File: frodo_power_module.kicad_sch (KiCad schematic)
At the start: 78 parts, among them J1 Keystone 1098, J10 SWD Header, J2 Molex MicroFit 2x2, J3 Molex MicroFit 2x2, J4 Molex MicroFit 2x2, J5 Molex MicroFit 2x2, J6 Molex MicroFit 2x2, J7 JST-GH, J8 JST-GH, J9 JST-GH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

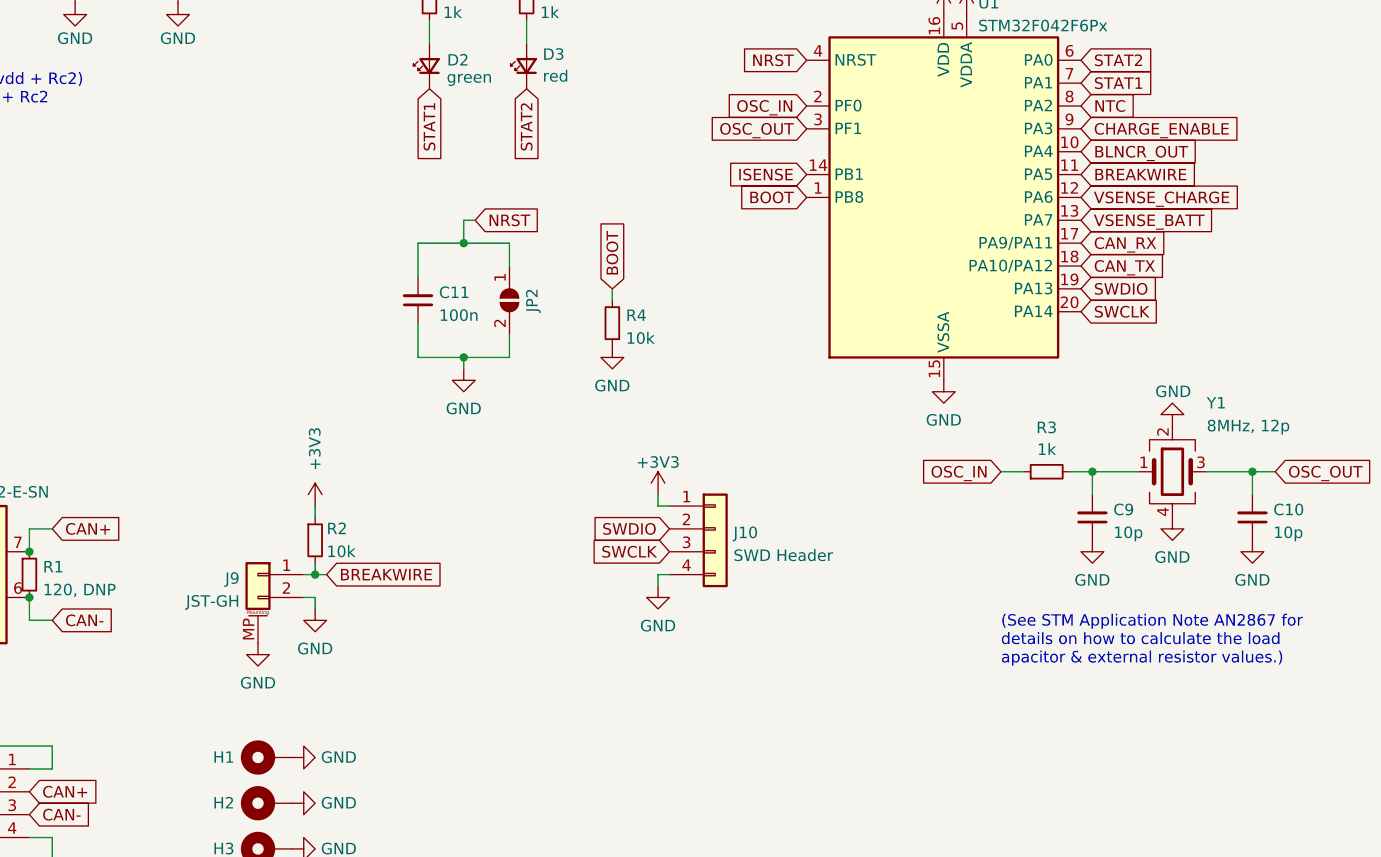
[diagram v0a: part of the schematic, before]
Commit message: removed breakwire system
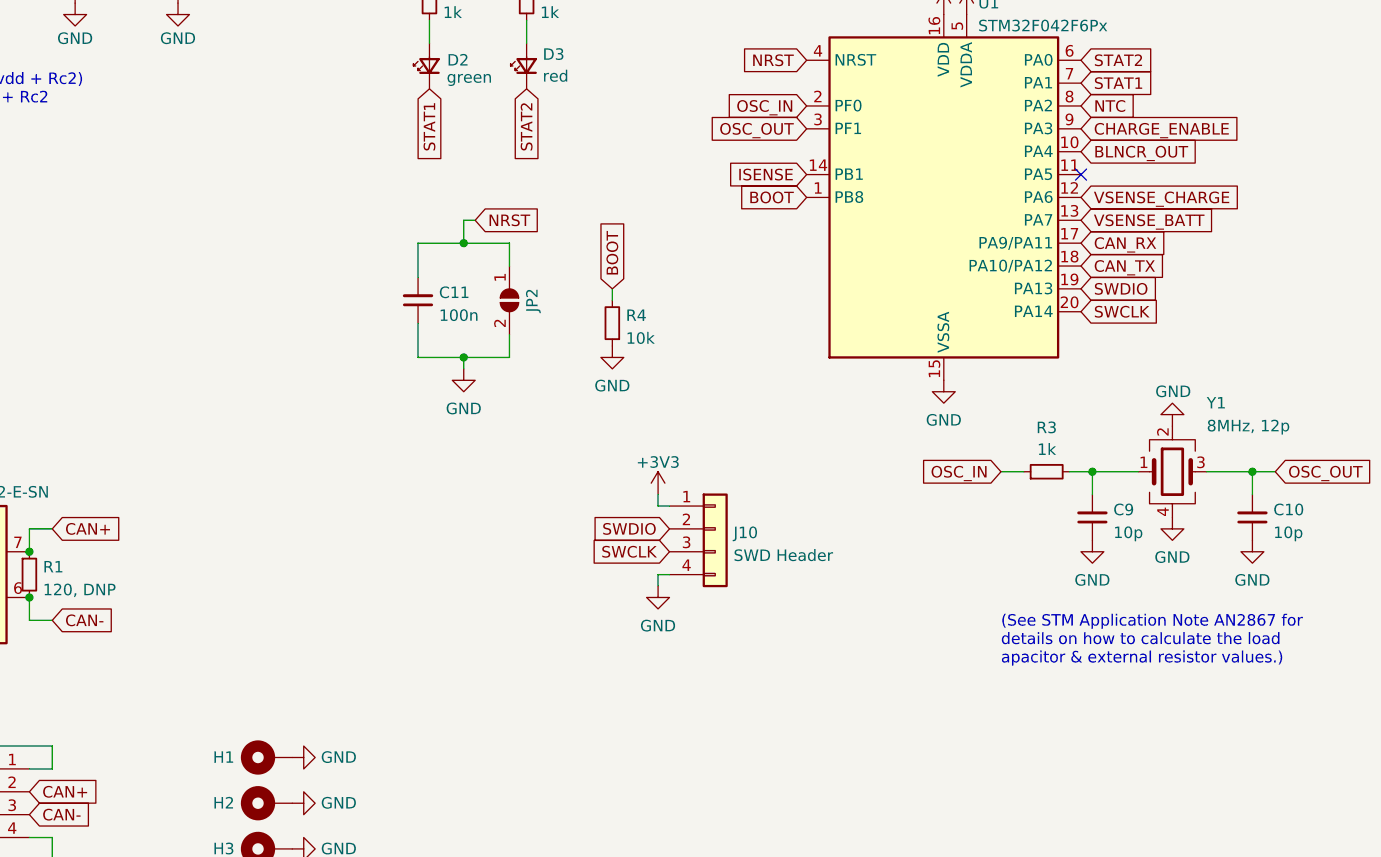
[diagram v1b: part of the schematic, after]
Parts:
- removed J9: JST-GH, Connector_JST:JST_GH_SM02B-GHS-TB_1x02-1MP_P1.25mm_Horizontal, symbol Connector_Generic_MountingPin:Conn_01x02_MountingPin
- removed R2: 10k, Resistor_SMD:R_0603_1608Metric, symbol Device:R_Small
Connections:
- net BREAKWIRE: no longer names the net of U1.11 (PA5)
- no-connect marks 0 -> 1
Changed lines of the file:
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@@
   (junction (at 44.45 161.29) (diameter 0) (color 0 0 0 0)
   )
-  (junction (at 165.1 152.4) (diameter 0) (color 0 0 0 0)
-  )
   (junction (at 205.74 31.75) (diameter 0) (color 0 0 0 0)
   )
@@
   (junction (at 44.45 154.94) (diameter 0) (color 0 0 0 0)
   )
+  (no_connect (at 250.19 107.95))
   (wire (pts (xy 135.89 181.61) (xy 135.89 184.15))
     (stroke (width 0) (type default))
@@
     (stroke (width 0) (type default))
   )
-  (wire (pts (xy 165.1 154.94) (xy 165.1 156.21))
-    (stroke (width 0) (type default))
-  )
   (wire (pts (xy 215.9 66.04) (xy 220.98 66.04))
     (stroke (width 0) (type default))
@@
     (stroke (width 0) (type default))
   )
-  (wire (pts (xy 165.1 151.13) (xy 165.1 152.4))
-    (stroke (width 0) (type default))
-  )
   (wire (pts (xy 220.98 76.2) (xy 220.98 77.47))
     (stroke (width 0) (type default))
@@
     (stroke (width 0) (type default))
   )
-  (wire (pts (xy 165.1 152.4) (xy 166.37 152.4))
-    (stroke (width 0) (type default))
-  )
   (wire (pts (xy 101.6 49.53) (xy 115.57 49.53))
     (stroke (width 0) (type default))
@@
     (stroke (width 0) (type default))
   )
-  (wire (pts (xy 163.83 152.4) (xy 165.1 152.4))
-    (stroke (width 0) (type default))
-  )
   (wire (pts (xy 44.45 176.53) (xy 44.45 177.8))
     (stroke (width 0) (type default))
@@
     (stroke (width 0) (type default))
   )
-  (wire (pts (xy 165.1 144.78) (xy 165.1 146.05))
-    (stroke (width 0) (type default))
-  )
   (wire (pts (xy 204.47 152.4) (xy 203.2 152.4))
     (stroke (width 0) (type default))
@@
     (stroke (width 0) (type default))
   )
-  (wire (pts (xy 163.83 154.94) (xy 165.1 154.94))
-    (stroke (width 0) (type default))
-  )
   (wire (pts (xy 21.59 67.31) (xy 21.59 71.12))
     (stroke (width 0) (type default))
@@
     )
   )
-  (global_label "BREAKWIRE" (shape input) (at 166.37 152.4 0) (fields_autoplaced)
-    (effects (font (size 1.27 1.27)) (justify left))
-    (property "Intersheetrefs" "${INTERSHEET_REFS}" (at 179.7986 152.4 0)
-      (effects (font (size 1.27 1.27)) (justify left) hide)
-    )
-  )
   (global_label "SWDIO" (shape input) (at 204.47 147.32 180) (fields_autoplaced)
     (effects (font (size 1.27 1.27)) (justify right))
@@
     )
   )
-  (global_label "BREAKWIRE" (shape input) (at 250.19 107.95 0) (fields_autoplaced)
-    (effects (font (size 1.27 1.27)) (justify left))
-    (property "Intersheetrefs" "${INTERSHEET_REFS}" (at 263.6186 107.95 0)
-      (effects (font (size 1.27 1.27)) (justify left) hide)
-    )
-  )
   (global_label "OSC_IN" (shape input) (at 219.71 100.33 180) (fields_autoplaced)
     (effects (font (size 1.27 1.27)) (justify right))
@@
     )
   )
-  (symbol (lib_id "Device:R_Small") (at 165.1 148.59 0) (unit 1)
-    (in_bom yes) (on_board yes) (dnp no)
-    (property "Reference" "R2" (at 166.37 147.32 0)
-      (effects (font (size 1.27 1.27)) (justify left))
-    )
-    (property "Value" "10k" (at 166.37 149.86 0)
-      (effects (font (size 1.27 1.27)) (justify left))
-    )
-    (property "Footprint" "Resistor_SMD:R_0603_1608Metric" (at 165.1 148.59 0)
-      (effects (font (size 1.27 1.27)) hide)
-    )
-    (property "Datasheet" "~" (at 165.1 148.59 0)
-      (effects (font (size 1.27 1.27)) hide)
-    )
-    (property "LCSC#" "C98220" (at 165.1 148.59 0)
-      (effects (font (size 1.27 1.27)) hide)
-    )
-    (property "Manufacturer" "YAGEO" (at 165.1 148.59 0)
-      (effects (font (size 1.27 1.27)) hide)
-    )
-    (property "Part#" "RC0603FR-0710KL" (at 165.1 148.59 0)
-      (effects (font (size 1.27 1.27)) hide)
-    )
-    (pin "1")
-    (pin "2")
-    (instances
-      (project "frodo_power_module"
-        (path "/afc8cbd3-9ea8-40a2-afae-ed6bd0fe7e6e"
-          (reference "R2") (unit 1)
-        )
-      )
-      (project "euroc_fc"
-        (path "/e63e39d7-6ac0-4ffd-8aa3-1841a4541b55"
-          (reference "R23") (unit 1)
-        )
-      )
-    )
-  )
   (symbol (lib_id "power:GND") (at 260.35 135.89 180) (unit 1)
     (in_bom yes) (on_board yes) (dnp no)
@@
     )
   )
-  (symbol (lib_id "power:+3V3") (at 165.1 144.78 0) (unit 1)
-    (in_bom yes) (on_board yes) (dnp no)
-    (property "Reference" "#PWR027" (at 165.1 148.59 0)
-      (effects (font (size 1.27 1.27)) hide)
-    )
-    (property "Value" "+3V3" (at 165.1 138.43 90)
-      (effects (font (size 1.27 1.27)))
-    )
-    (property "Footprint" "" (at 165.1 144.78 0)
-      (effects (font (size 1.27 1.27)) hide)
-    )
-    (property "Datasheet" "" (at 165.1 144.78 0)
-      (effects (font (size 1.27 1.27)) hide)
-    )
-    (pin "1")
-    (instances
-      (project "frodo_power_module"
-        (path "/afc8cbd3-9ea8-40a2-afae-ed6bd0fe7e6e"
-          (reference "#PWR027") (unit 1)
-        )
-      )
-      (project "euroc_fc"
-        (path "/e63e39d7-6ac0-4ffd-8aa3-1841a4541b55"
-          (reference "#PWR029") (unit 1)
-        )
-      )
-    )
-  )
   (symbol (lib_id "Regulator_Linear:AZ1117-3.3") (at 255.27 27.94 0) (unit 1)
     (in_bom yes) (on_board yes) (dnp no) (fields_autoplaced)
@@
     )
   )
-  (symbol (lib_id "power:GND") (at 165.1 156.21 0) (mirror y) (unit 1)
-    (in_bom yes) (on_board yes) (dnp no) (fields_autoplaced)
-    (property "Reference" "#PWR035" (at 165.1 162.56 0)
-      (effects (font (size 1.27 1.27)) hide)
-    )
-    (property "Value" "GND" (at 165.1 160.6534 0)
-      (effects (font (size 1.27 1.27)))
-    )
-    (property "Footprint" "" (at 165.1 156.21 0)
-      (effects (font (size 1.27 1.27)) hide)
-    )
-    (property "Datasheet" "" (at 165.1 156.21 0)
-      (effects (font (size 1.27 1.27)) hide)
-    )
-    (pin "1")
-    (instances
-      (project "frodo_power_module"
-        (path "/afc8cbd3-9ea8-40a2-afae-ed6bd0fe7e6e"
-          (reference "#PWR035") (unit 1)
-        )
-      )
-      (project "euroc_fc"
-        (path "/e63e39d7-6ac0-4ffd-8aa3-1841a4541b55"
-          (reference "#PWR0169") (unit 1)
-        )
-      )
-    )
-  )
   (symbol (lib_id "power:+VSW") (at 45.72 161.29 270) (mirror x) (unit 1)
     (in_bom yes) (on_board yes) (dnp no) (fields_autoplaced)
@@
     )
   )
-  (symbol (lib_id "Connector_Generic_MountingPin:Conn_01x02_MountingPin") (at 158.75 152.4 0) (mirror y) (unit 1)
-    (in_bom yes) (on_board yes) (dnp no) (fields_autoplaced)
-    (property "Reference" "J9" (at 156.718 152.8353 0)
-      (effects (font (size 1.27 1.27)) (justify left))
-    )
-    (property "Value" "JST-GH" (at 156.718 155.3722 0)
-      (effects (font (size 1.27 1.27)) (justify left))
-    )
-    (property "Footprint" "Connector_JST:JST_GH_SM02B-GHS-TB_1x02-1MP_P1.25mm_Horizontal" (at 158.75 152.4 0)
-      (effects (font (size 1.27 1.27)) hide)
-    )
-    (property "Datasheet" "~" (at 158.75 152.4 0)
-      (effects (font (size 1.27 1.27)) hide)
-    )
-    (property "LCSC#" "C189893" (at 158.75 152.4 0)
-      (effects (font (size 1.27 1.27)) hide)
-    )
-    (property "Manufacturer" "JST" (at 158.75 152.4 0)
-      (effects (font (size 1.27 1.27)) hide)
-    )
-    (property "Part#" "SM02B-GHS-TB" (at 158.75 152.4 0)
-      (effects (font (size 1.27 1.27)) hide)
-    )
-    (pin "1")
-    (pin "2")
-    (pin "MP")
-    (instances
-      (project "frodo_power_module"
-        (path "/afc8cbd3-9ea8-40a2-afae-ed6bd0fe7e6e"
-          (reference "J9") (unit 1)
-        )
-      )
-      (project "euroc_fc"
-        (path "/e63e39d7-6ac0-4ffd-8aa3-1841a4541b55"
-          (reference "J6") (unit 1)
-        )
-      )
-    )
-  )
   (symbol (lib_id "Device:C_Small") (at 176.53 121.92 180) (unit 1)
     (in_bom yes) (on_board yes) (dnp no)
@@
         )
       )
-    )
-  )
-  (symbol (lib_id "power:GND") (at 158.75 160.02 0) (mirror y) (unit 1)
-    (in_bom yes) (on_board yes) (dnp no) (fields_autoplaced)
-    (property "Reference" "#PWR020" (at 158.75 166.37 0)
-      (effects (font (size 1.27 1.27)) hide)
-    )
-    (property "Value" "GND" (at 158.75 164.4634 0)
-      (effects (font (size 1.27 1.27)))
-    )
-    (property "Footprint" "" (at 158.75 160.02 0)
-      (effects (font (size 1.27 1.27)) hide)
-    )
-    (property "Datasheet" "" (at 158.75 160.02 0)
-      (effects (font (size 1.27 1.27)) hide)
-    )
-    (pin "1")
-    (instances
-      (project "frodo_power_module"
-        (path "/afc8cbd3-9ea8-40a2-afae-ed6bd0fe7e6e"
-          (reference "#PWR020") (unit 1)
-        )
-      )
-      (project "euroc_fc"
-        (path "/e63e39d7-6ac0-4ffd-8aa3-1841a4541b55"
-          (reference "#PWR0169") (unit 1)
-        )
-      )

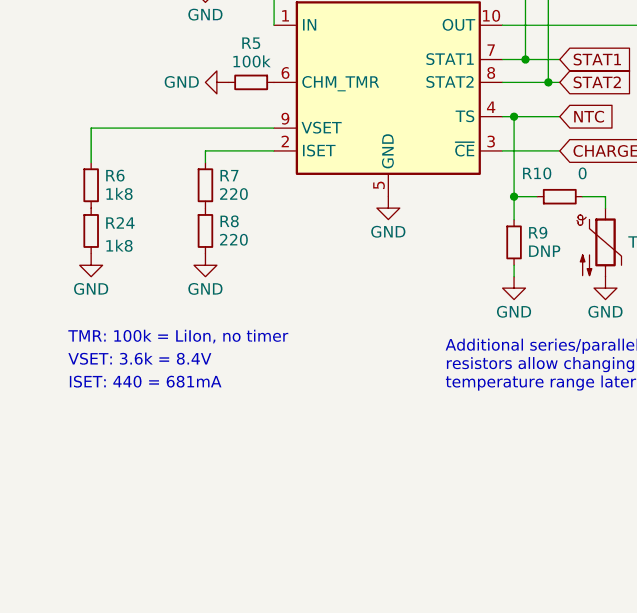
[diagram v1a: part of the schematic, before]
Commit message: removed breakwire and changed Iset resistance from 440 to 390 to achieve approx 800mA charging
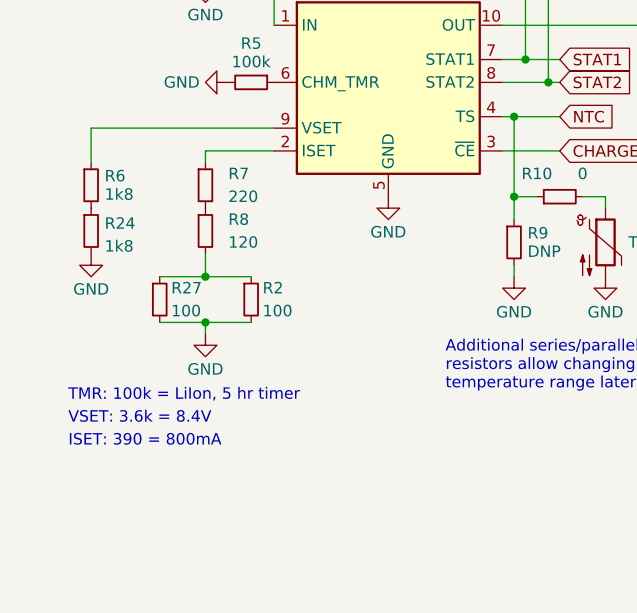
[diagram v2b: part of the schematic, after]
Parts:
- added R2, R27: 100, Resistor_SMD:R_0603_1608Metric, symbol Device:R_Small
- R8: value 220 -> 120
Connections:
- net GND: now also R2.2, R27.2; no longer R8.2
- new net: R2.1, R27.1, R8.2
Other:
- note added: "ISET: 390 = 800mA"
- note added: "TMR: 100k = LiIon, 5 hr timer"
- note removed: "ISET: 440 = 681mA"
- note removed: "TMR: 100k = LiIon, no timer"
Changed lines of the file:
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@@
   (junction (at 223.52 31.75) (diameter 0) (color 0 0 0 0)
   )
+  (junction (at 34.29 83.82) (diameter 0) (color 0 0 0 0)
+  )
   (junction (at 133.35 154.94) (diameter 0) (color 0 0 0 0)
   )
@@
   (junction (at 251.46 140.97) (diameter 0) (color 0 0 0 0)
   )
+  (junction (at 34.29 88.9) (diameter 0) (color 0 0 0 0)
+  )
   (junction (at 165.1 67.31) (diameter 0) (color 0 0 0 0)
   )
@@
     (stroke (width 0) (type default))
   )
+  (wire (pts (xy 34.29 88.9) (xy 34.29 90.17))
+    (stroke (width 0) (type default))
+  )
+  (wire (pts (xy 34.29 83.82) (xy 39.37 83.82))
+    (stroke (width 0) (type default))
+  )
   (wire (pts (xy 121.92 62.23) (xy 121.92 64.77))
     (stroke (width 0) (type default))
@@
     (stroke (width 0) (type default))
   )
+  (wire (pts (xy 29.21 88.9) (xy 34.29 88.9))
+    (stroke (width 0) (type default))
+  )
   (wire (pts (xy 76.2 74.93) (xy 78.74 74.93))
     (stroke (width 0) (type default))
@@
     (stroke (width 0) (type default))
   )
+  (wire (pts (xy 34.29 81.28) (xy 34.29 83.82))
+    (stroke (width 0) (type default))
+  )
   (wire (pts (xy 245.11 76.2) (xy 245.11 73.66))
     (stroke (width 0) (type default))
@@
     (stroke (width 0) (type default))
   )
+  (wire (pts (xy 34.29 88.9) (xy 39.37 88.9))
+    (stroke (width 0) (type default))
+  )
+  (wire (pts (xy 29.21 83.82) (xy 34.29 83.82))
+    (stroke (width 0) (type default))
+  )
   (wire (pts (xy 242.57 25.4) (xy 242.57 27.94))
     (stroke (width 0) (type default))
@@
     (effects (font (size 1.27 1.27)) (justify left bottom))
   )
-  (text "TMR: 100k = LiIon, no timer" (at 19.05 91.44 0)
+  (text "TMR: 100k = LiIon, 5 hr timer\n" (at 19.05 97.79 0)
     (effects (font (size 1.27 1.27)) (justify left bottom))
   )
-  (text "VSET: 3.6k = 8.4V" (at 19.05 93.98 0)
+  (text "VSET: 3.6k = 8.4V" (at 19.05 100.33 0)
     (effects (font (size 1.27 1.27)) (justify left bottom))
   )
@@
     (effects (font (size 1.27 1.27)) (justify left bottom))
   )
-  (text "ISET: 440 = 681mA" (at 19.05 96.52 0)
+  (text "ISET: 390 = 800mA" (at 19.05 102.87 0)
     (effects (font (size 1.27 1.27)) (justify left bottom))
   )
@@
     )
   )
+  (symbol (lib_id "Device:R_Small") (at 39.37 86.36 0) (unit 1)
+    (in_bom yes) (on_board yes) (dnp no)
+    (property "Reference" "R2" (at 40.64 85.09 0)
+      (effects (font (size 1.27 1.27)) (justify left))
+    )
+    (property "Value" "100" (at 40.64 87.63 0)
+      (effects (font (size 1.27 1.27)) (justify left))
+    )
+    (property "Footprint" "Resistor_SMD:R_0603_1608Metric" (at 39.37 86.36 0)
+      (effects (font (size 1.27 1.27)) hide)
+    )
+    (property "Datasheet" "~" (at 39.37 86.36 0)
+      (effects (font (size 1.27 1.27)) hide)
+    )
+    (property "Manufacturer" "YAGEO" (at 39.37 86.36 0)
+      (effects (font (size 1.27 1.27)) hide)
+    )
+    (property "Part#" "RC0603FR-07220RL" (at 39.37 86.36 0)
+      (effects (font (size 1.27 1.27)) hide)
+    )
+    (property "LCSC#" "C107696" (at 39.37 86.36 0)
+      (effects (font (size 1.27 1.27)) hide)
+    )
+    (pin "1")
+    (pin "2")
+    (instances
+      (project "frodo_power_module"
+        (path "/afc8cbd3-9ea8-40a2-afae-ed6bd0fe7e6e"
+          (reference "R2") (unit 1)
+        )
+      )
+      (project "euroc_fc"
+        (path "/e63e39d7-6ac0-4ffd-8aa3-1841a4541b55"
+          (reference "R6") (unit 1)
+        )
+      )
+    )
+  )
   (symbol (lib_id "power:GND") (at 138.43 88.9 0) (unit 1)
     (in_bom yes) (on_board yes) (dnp no) (fields_autoplaced)
@@
   )
   (symbol (lib_id "Device:R_Small") (at 34.29 73.66 0) (unit 1)
-    (in_bom yes) (on_board yes) (dnp no) (fields_autoplaced)
-    (property "Reference" "R7" (at 35.7886 72.636 0)
+    (in_bom yes) (on_board yes) (dnp no)
+    (property "Reference" "R7" (at 36.83 72.39 0)
       (effects (font (size 1.27 1.27)) (justify left))
     )
-    (property "Value" "220" (at 35.7886 74.684 0)
+    (property "Value" "220" (at 36.83 74.93 0)
       (effects (font (size 1.27 1.27)) (justify left))
     )
@@
     )
   )
-  (symbol (lib_id "power:GND") (at 34.29 81.28 0) (unit 1)
+  (symbol (lib_id "power:GND") (at 34.29 90.17 0) (unit 1)
     (in_bom yes) (on_board yes) (dnp no) (fields_autoplaced)
-    (property "Reference" "#PWR059" (at 34.29 87.63 0)
+    (property "Reference" "#PWR059" (at 34.29 96.52 0)
       (effects (font (size 1.27 1.27)) hide)
     )
-    (property "Value" "GND" (at 34.29 85.225 0)
+    (property "Value" "GND" (at 34.29 94.115 0)
       (effects (font (size 1.27 1.27)))
     )
-    (property "Footprint" "" (at 34.29 81.28 0)
+    (property "Footprint" "" (at 34.29 90.17 0)
       (effects (font (size 1.27 1.27)) hide)
     )
-    (property "Datasheet" "" (at 34.29 81.28 0)
+    (property "Datasheet" "" (at 34.29 90.17 0)
       (effects (font (size 1.27 1.27)) hide)
     )
@@
     )
   )
+  (symbol (lib_id "Device:R_Small") (at 29.21 86.36 0) (unit 1)
+    (in_bom yes) (on_board yes) (dnp no)
+    (property "Reference" "R27" (at 30.48 85.09 0)
+      (effects (font (size 1.27 1.27)) (justify left))
+    )
+    (property "Value" "100" (at 30.48 87.63 0)
+      (effects (font (size 1.27 1.27)) (justify left))
+    )
+    (property "Footprint" "Resistor_SMD:R_0603_1608Metric" (at 29.21 86.36 0)
+      (effects (font (size 1.27 1.27)) hide)
+    )
+    (property "Datasheet" "~" (at 29.21 86.36 0)
+      (effects (font (size 1.27 1.27)) hide)
+    )
+    (property "Manufacturer" "YAGEO" (at 29.21 86.36 0)
+      (effects (font (size 1.27 1.27)) hide)
+    )
+    (property "Part#" "RC0603FR-07220RL" (at 29.21 86.36 0)
+      (effects (font (size 1.27 1.27)) hide)
+    )
+    (property "LCSC#" "C107696" (at 29.21 86.36 0)
+      (effects (font (size 1.27 1.27)) hide)
+    )
+    (pin "1")
+    (pin "2")
+    (instances
+      (project "frodo_power_module"
+        (path "/afc8cbd3-9ea8-40a2-afae-ed6bd0fe7e6e"
+          (reference "R27") (unit 1)
+        )
+      )
+      (project "euroc_fc"
+        (path "/e63e39d7-6ac0-4ffd-8aa3-1841a4541b55"
+          (reference "R6") (unit 1)
+        )
+      )
+    )
+  )
   (symbol (lib_id "Device:C_Small") (at 255.27 71.12 180) (unit 1)
     (in_bom yes) (on_board yes) (dnp no)
@@
   (symbol (lib_id "Device:R_Small") (at 34.29 78.74 0) (unit 1)
     (in_bom yes) (on_board yes) (dnp no) (fields_autoplaced)
-    (property "Reference" "R8" (at 35.7886 77.716 0)
+    (property "Reference" "R8" (at 36.83 77.47 0)
       (effects (font (size 1.27 1.27)) (justify left))
     )
-    (property "Value" "220" (at 35.7886 79.764 0)
+    (property "Value" "120" (at 36.83 80.01 0)
       (effects (font (size 1.27 1.27)) (justify left))
     )
